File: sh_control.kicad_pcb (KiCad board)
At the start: 2 copper layers, 21 parts, among them J1 USB_PORT_1, J2 USB_Port_2, J3 USB_Port_3, J4 USB_Port_4, U1 FE1.1s, Y1 X322512MSB4SI

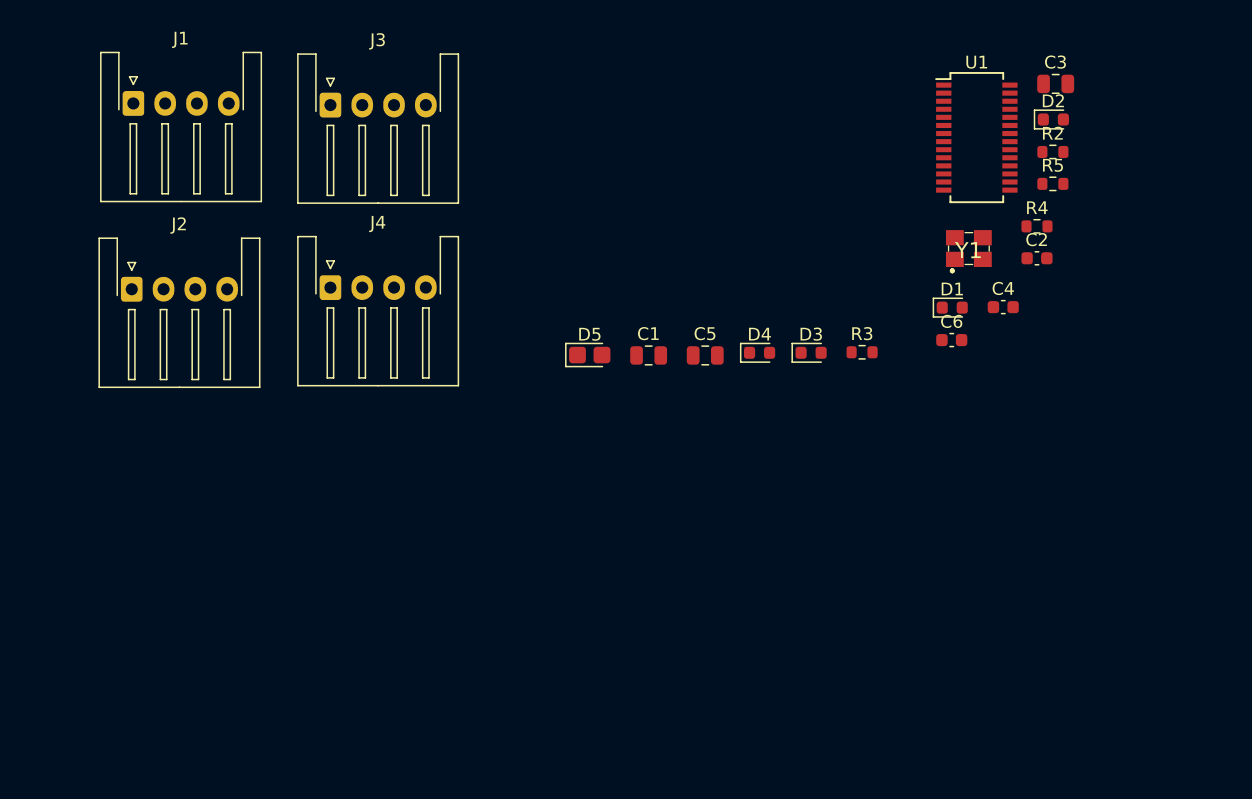
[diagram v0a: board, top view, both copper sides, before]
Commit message: added atmega32 schematic
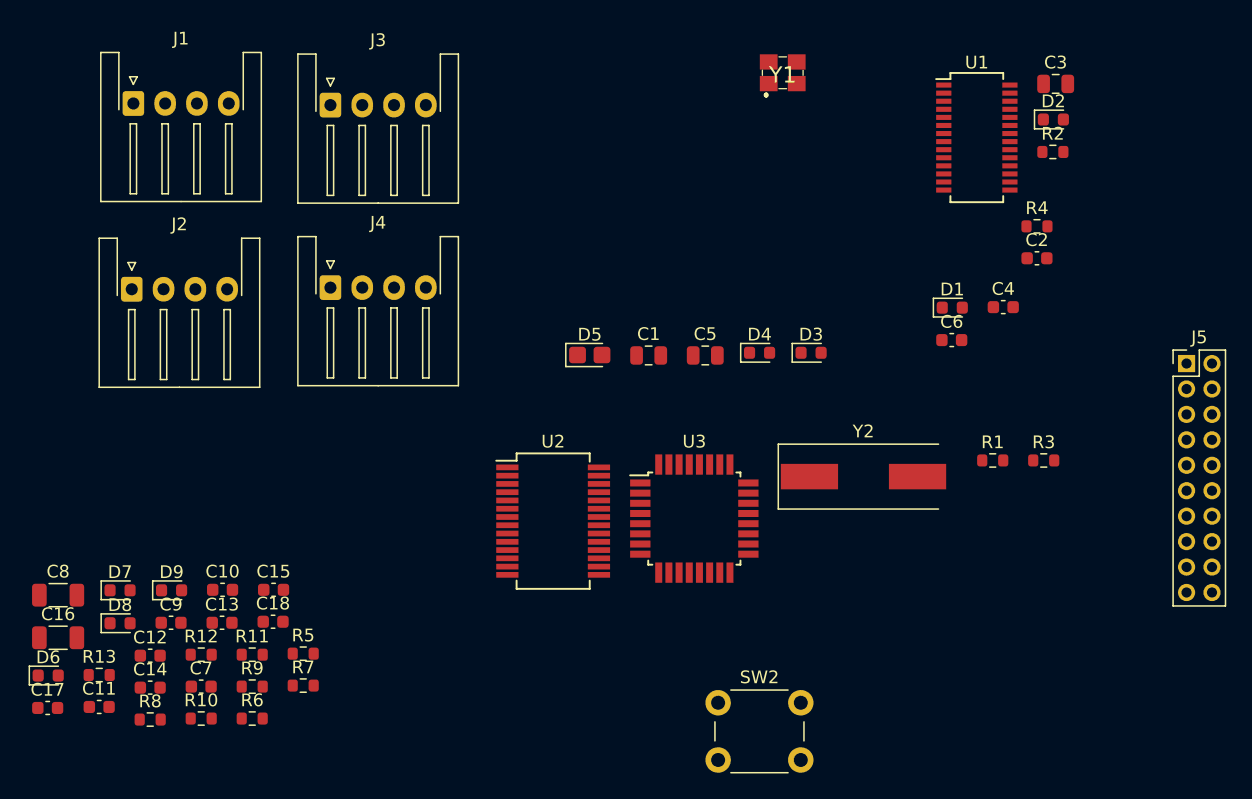
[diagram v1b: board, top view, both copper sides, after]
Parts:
- added C10: 100nF, Capacitor_SMD:C_0603_1608Metric, F.Cu at (113.4, 147.3)
- added C11: 22pF, Capacitor_SMD:C_0603_1608Metric, F.Cu at (103.7, 156.5)
- added C12: 22pF, Capacitor_SMD:C_0603_1608Metric, F.Cu at (107.8, 152.5)
- added C13: 22pF, Capacitor_SMD:C_0603_1608Metric, F.Cu at (113.4, 149.9)
- added C14: 22pF, Capacitor_SMD:C_0603_1608Metric, F.Cu at (107.8, 155.0)
- added C15: 100nF, Capacitor_SMD:C_0603_1608Metric, F.Cu at (117.5, 147.3)
- added C16: 4.7uF, Capacitor_SMD:C_1206_3216Metric, F.Cu at (100.5, 151.1)
- added C17: 100nF, Capacitor_SMD:C_0603_1608Metric, F.Cu at (99.7, 156.6)
- added C18: 100nF, Capacitor_SMD:C_0603_1608Metric, F.Cu at (117.4, 149.8)
- added C7: 100nF, Capacitor_SMD:C_0603_1608Metric, F.Cu at (111.8, 154.9)
- added C8: 4.7uF, Capacitor_SMD:C_1206_3216Metric, F.Cu at (100.5, 147.8)
- added C9: 100nF, Capacitor_SMD:C_0603_1608Metric, F.Cu at (109.4, 149.9)
- added D6: SCK, LED_SMD:LED_0603_1608Metric, F.Cu at (99.7, 154.1)
- added D7: 3V3, LED_SMD:LED_0603_1608Metric, F.Cu at (105.4, 147.4)
- added D8: RX, LED_SMD:LED_0603_1608Metric, F.Cu at (105.4, 150.0)
- added D9: TX, LED_SMD:LED_0603_1608Metric, F.Cu at (109.4, 147.4)
- added J5: Conn_02x10_Odd_Even, Connector_PinHeader_2.00mm:PinHeader_2x10_P2.00mm_Vertical, F.Cu at (189.2, 129.5)
- added R1: 1.5K, Resistor_SMD:R_0603_1608Metric, F.Cu at (174.0, 137.2)
- added R10: 22, Resistor_SMD:R_0603_1608Metric, F.Cu at (111.8, 157.4)
- added R11: 1K, Resistor_SMD:R_0603_1608Metric, F.Cu at (115.8, 152.4)
- added R12: 1K, Resistor_SMD:R_0603_1608Metric, F.Cu at (111.8, 152.4)
- added R13: 1K, Resistor_SMD:R_0603_1608Metric, F.Cu at (103.7, 154.0)
- added R6: 1K, Resistor_SMD:R_0603_1608Metric, F.Cu at (115.8, 157.4)
- added R7: 1K, Resistor_SMD:R_0603_1608Metric, F.Cu at (119.8, 154.9)
- added R8: 1K, Resistor_SMD:R_0603_1608Metric, F.Cu at (107.8, 157.5)
- added R9: 22, Resistor_SMD:R_0603_1608Metric, F.Cu at (115.8, 154.9)
- added SW2: SW_Push_Dual_x2, Button_Switch_THT:SW_PUSH_6mm_H4.3mm, F.Cu at (152.4, 156.2)
- added U2: FT232RL, Package_SO:SSOP-28_5.3x10.2mm_P0.65mm, F.Cu at (139.4, 141.9)
- added U3: ATmega328P-AU, Package_QFP:TQFP-32_7x7mm_P0.8mm, F.Cu at (150.5, 141.7)
- added Y2: Crystal, Crystal:Crystal_SMD_HC49-SD, F.Cu at (163.8, 138.4)
- R3, R4: value 1K -> 1.5K
- Y1: footprint crystal_12MHz:X322512MSB4SI -> max_KiCAD_lib:X322512MSB4SI
- moved R5 69.6 mm to (119.8, 152.3)
- moved Y1 20.1 mm to (157.5, 106.7)
- moved R3 16.6 mm to (178.0, 137.2)
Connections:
- D1 pad 1: Net-(D1-Pad1) -> /USB_HUB/DRV
- D2 pad 2: Net-(D1-Pad1) -> /USB_HUB/DRV
- D3 pad 1: Net-(D1-Pad1) -> /USB_HUB/DRV
- D4 pad 2: Net-(D1-Pad1) -> /USB_HUB/DRV
- D5 pad 1: GND -> Net-(D5-Pad1)
- D5 pad 2: Net-(D5-Pad2) -> /USB_HUB/DRV
- R3 pad 1: Net-(D1-Pad2) -> GND
- R3 pad 2: /USB_HUB/LED1 -> Net-(D5-Pad1)
- R5 pad 1: Net-(D5-Pad2) -> Net-(R5-Pad1)
- R5 pad 2: Net-(D1-Pad1) -> /Atmega32/TXD

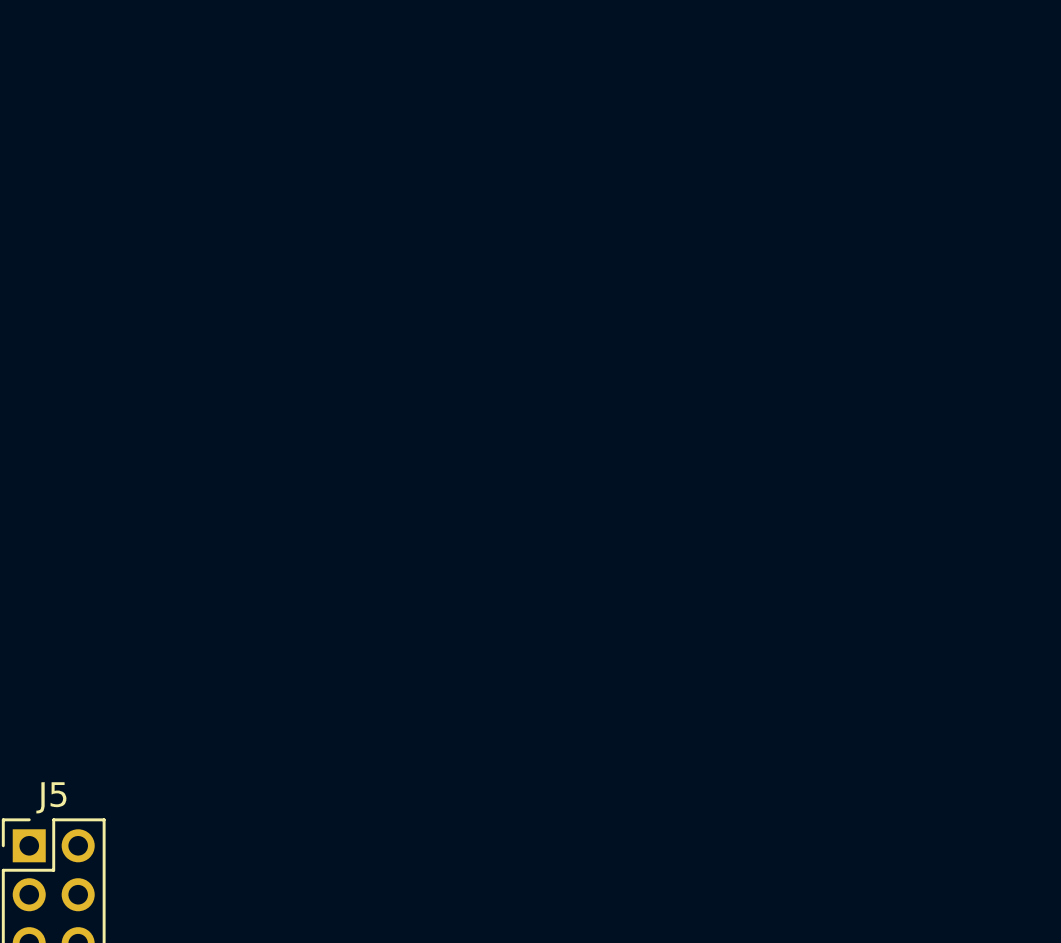
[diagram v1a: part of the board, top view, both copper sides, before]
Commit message: small changes to schematic
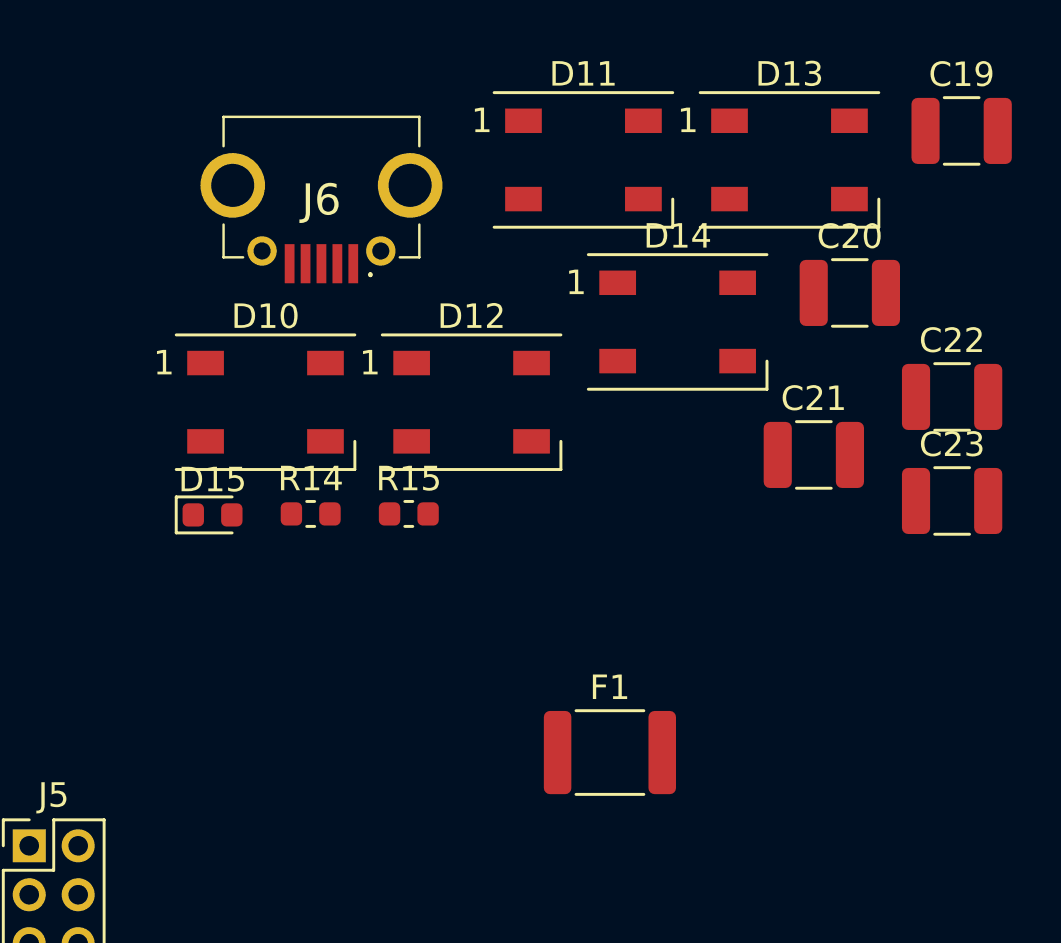
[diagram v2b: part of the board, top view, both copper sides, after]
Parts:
- added C19: 100 uF, Capacitor_SMD:C_1210_3225Metric, F.Cu at (227.3, 100.3)
- added C20: 100 uF, Capacitor_SMD:C_1210_3225Metric, F.Cu at (222.8, 107.0)
- added C21: 100 uF, Capacitor_SMD:C_1210_3225Metric, F.Cu at (221.3, 113.6)
- added C22: 100 uF, Capacitor_SMD:C_1210_3225Metric, F.Cu at (226.9, 111.2)
- added C23: 100 uF, Capacitor_SMD:C_1210_3225Metric, F.Cu at (226.9, 115.5)
- added D10: WS2812B, LED_SMD:LED_WS2812B_PLCC4_5.0x5.0mm_P3.2mm, F.Cu at (198.9, 111.4)
- added D11: WS2812B, LED_SMD:LED_WS2812B_PLCC4_5.0x5.0mm_P3.2mm, F.Cu at (211.9, 101.5)
- added D12: WS2812B, LED_SMD:LED_WS2812B_PLCC4_5.0x5.0mm_P3.2mm, F.Cu at (207.3, 111.4)
- added D13: WS2812B, LED_SMD:LED_WS2812B_PLCC4_5.0x5.0mm_P3.2mm, F.Cu at (220.3, 101.5)
- added D14: WS2812B, LED_SMD:LED_WS2812B_PLCC4_5.0x5.0mm_P3.2mm, F.Cu at (215.7, 108.1)
- added D15: LED_Small, LED_SMD:LED_0603_1608Metric, F.Cu at (196.7, 116.0)
- added F1: 500 mA, Fuse:Fuse_1812_4532Metric, F.Cu at (213.0, 125.7)
- added J6: C10418, max_KiCAD_lib:C10418, F.Cu at (201.2, 102.8)
- added R14: 1.5K, Fuse:Fuse_0603_1608Metric, F.Cu at (200.7, 116.0)
- added R15: 300, Fuse:Fuse_0603_1608Metric, F.Cu at (204.7, 116.0)
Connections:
- C13 pad 1: /Atmega32/D+ -> /Atmega32/D_P
- C14 pad 1: /Atmega32/D- -> /Atmega32/D_N
- J4 pad 3: /USB_HUB/D4_P -> /D4_P
- J4 pad 4: /USB_HUB/D4_N -> /D4_N
- J5 pad 17: Net-(J5-Pad17) -> /D4_P
- J5 pad 18: Net-(J5-Pad18) -> /Atmega32/D_P
- J5 pad 19: Net-(J5-Pad19) -> /D4_N
- J5 pad 20: Net-(J5-Pad20) -> /Atmega32/D_N
- R10 pad 1: /Atmega32/D- -> /Atmega32/D_N
- R9 pad 1: /Atmega32/D+ -> /Atmega32/D_P
- U1 pad 15: /USB_HUB/D_M -> /D_N
- U1 pad 16: /USB_HUB/D_P -> /D_P
- U1 pad 4: /USB_HUB/D4_N -> /D4_N
- U1 pad 5: /USB_HUB/D4_P -> /D4_P
- U3 pad 9: Net-(U3-Pad9) -> /data

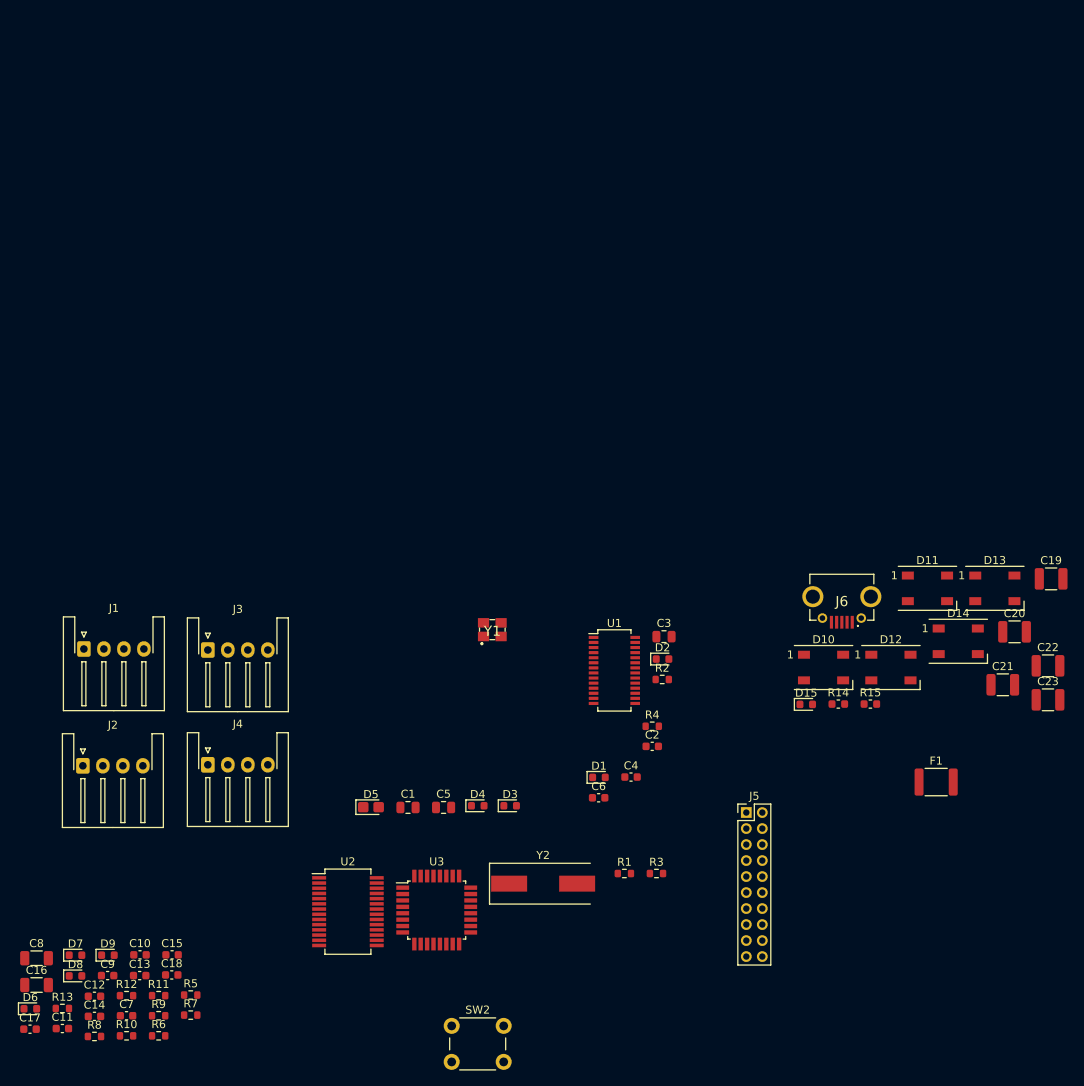
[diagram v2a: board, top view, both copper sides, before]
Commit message: pcb schematic and layout edit i.e. finished -> orderd pcb jlcpcb
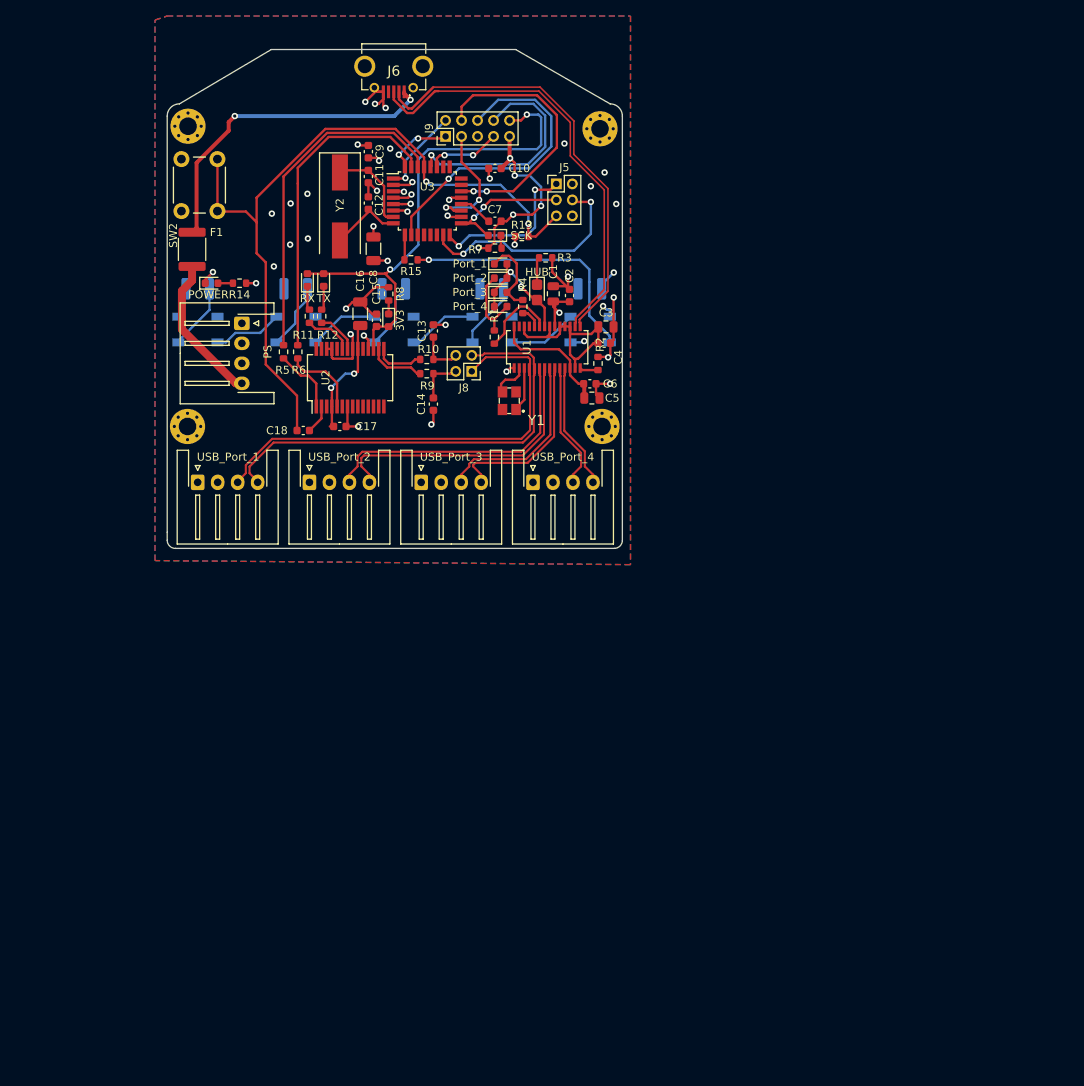
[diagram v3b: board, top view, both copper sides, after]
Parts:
- added J7: PS, Connector_JST:JST_XH_S4B-XH-A-1_1x04_P2.50mm_Horizontal, F.Cu at (126.2, 68.4)
- added J8: Conn_02x02_Odd_Even, Connector_PinHeader_2.00mm:PinHeader_2x02_P2.00mm_Vertical, F.Cu at (154.9, 74.4)
- added J9: Conn_02x05_Odd_Even, Connector_PinHeader_2.00mm:PinHeader_2x05_P2.00mm_Vertical, F.Cu at (151.6, 45.0)
- added TP1: TestPoint, MountingHole:MountingHole_2.2mm_M2_Pad_Via, F.Cu at (171.2, 81.3)
- added TP2: TestPoint, MountingHole:MountingHole_2.2mm_M2_Pad_Via, F.Cu at (170.9, 44.1)
- added TP3: TestPoint, MountingHole:MountingHole_2.2mm_M2_Pad_Via, F.Cu at (119.4, 43.8)
- added TP4: TestPoint, MountingHole:MountingHole_2.2mm_M2_Pad_Via, F.Cu at (119.4, 81.3)
- C19, C20, C21, C22, C23, D10, D11, D12, D13, D14: moved to B.Cu
- D15: value LED_Small -> POWER
- J1: value USB_PORT_1 -> USB_Port_1
- J5: value Conn_02x10_Odd_Even -> Conn_02x03_Odd_Even; footprint Connector_PinHeader_2.00mm:PinHeader_2x10_P2.00mm_Vertical -> Connector_PinHeader_2.00mm:PinHeader_2x03_P2.00mm_Vertical
- R14, R15: footprint Fuse:Fuse_0603_1608Metric -> Resistor_SMD:R_0603_1608Metric
- moved C23 118.1 mm to (120.7, 64.1), turned to 180 degrees
- moved F1 114.4 mm to (120.0, 59.1), turned to 90 degrees
- moved C11 113.2 mm to (142.0, 50.0), turned to 270 degrees
- moved D6 112.8 mm to (157.8, 57.4), turned to 180 degrees
- moved R13 112.3 mm to (161.2, 57.5)
- moved C7 109.5 mm to (157.8, 55.6)
- moved C9 108.0 mm to (142.0, 46.9), turned to 270 degrees
- moved C10 107.9 mm to (157.8, 49.0)
- moved SW2 107.3 mm to (118.6, 54.4), turned to 90 degrees
- moved C22 105.2 mm to (132.9, 64.1), turned to 180 degrees
- moved C12 104.9 mm to (142.0, 53.4), turned to 90 degrees
- moved R7 103.1 mm to (157.8, 59.0), turned to 180 degrees
- moved D14 102.7 mm to (120.7, 69.2)
- moved R8 99.8 mm to (144.5, 64.7), turned to 270 degrees
- moved C8 98.2 mm to (142.6, 59.1), turned to 90 degrees
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- renumbered D7 to 3V3
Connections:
- 3V3 pad 2: +3V3 -> /Atmega32/3V3_ft232rl
- C15 pad 2: +3V3 -> /Atmega32/3V3_ft232rl
- C9 pad 1: GND -> Net-(C9-Pad1)
- C9 pad 2: +5V -> Net-(C9-Pad2)
- D1 pad 1: /USB_HUB/DRV -> Net-(D1-Pad1)
- D1 pad 2: Net-(D1-Pad2) -> /USB_HUB/DRV
- D2 pad 1: Net-(D1-Pad2) -> /USB_HUB/DRV
- D2 pad 2: /USB_HUB/DRV -> Net-(D1-Pad1)
- D3 pad 1: /USB_HUB/DRV -> Net-(D3-Pad1)
- D3 pad 2: Net-(D3-Pad2) -> /USB_HUB/DRV
- D4 pad 1: Net-(D3-Pad2) -> /USB_HUB/DRV
- D4 pad 2: /USB_HUB/DRV -> Net-(D3-Pad1)
- D8 pad 2: +3V3 -> /Atmega32/3V3_ft232rl
- D9 pad 2: +3V3 -> /Atmega32/3V3_ft232rl
- F1 pad 1: +5V -> Net-(F1-Pad1)
- J1 pad 3: /USB_HUB/D1_P -> /D4_N
- J1 pad 4: /USB_HUB/D1_N -> /D4_P
- J2 pad 3: /USB_HUB/D2_P -> /USB_HUB/D3_N
- J2 pad 4: /USB_HUB/D2_N -> /USB_HUB/D3_P
- J3 pad 3: /USB_HUB/D3_P -> /USB_HUB/D2_N
- J3 pad 4: /USB_HUB/D3_N -> /USB_HUB/D2_P
- J4 pad 3: /D4_P -> /USB_HUB/D1_N
- J4 pad 4: /D4_N -> /USB_HUB/D1_P
- R1 pad 1: Net-(D1-Pad2) -> Net-(D3-Pad1)
- R4 pad 1: Net-(D3-Pad2) -> Net-(D1-Pad1)
- U2 pad 17: +3V3 -> /Atmega32/3V3_ft232rl
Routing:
- net GND: track 0.00 -> 95.8 mm, vias 0 -> 37
- net /Atmega32/RESET: track 0.00 -> 94.2 mm, vias 0 -> 2
- net /Atmega32/3V3_ft232rl: track 0.00 -> 62.0 mm, vias 0 -> 2
- net /D4_P: track 0.00 -> 58.1 mm
- net /D4_N: track 0.00 -> 58.0 mm
- net /D_P: track 0.00 -> 55.3 mm
- net /D_N: track 0.00 -> 55.1 mm
- net Net-(R5-Pad1): track 0.00 -> 42.6 mm
- net Net-(F1-Pad2): track 0.00 -> 40.9 mm, vias 0 -> 2
- net Net-(R6-Pad1): track 0.00 -> 40.2 mm
- net /Atmega32/PD6: track 0.00 -> 38.4 mm, vias 0 -> 1
- net +5V: track 0.00 -> 38.2 mm, vias 0 -> 12
- net /USB_HUB/D3_P: track 0.00 -> 36.9 mm
- net /USB_HUB/D3_N: track 0.00 -> 36.9 mm
- net /Atmega32/ADC7: track 0.00 -> 33.5 mm, vias 0 -> 2
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- added copper zone on In1.Cu, net +5V
- added copper zone on B.Cu, net GND
- added copper zone on F.Cu, net GND
- added copper zone on In2.Cu, net GND
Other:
- board outline added: 56.9 x 62.4 mm
- copper layers 2 -> 4
- board text added: "Stiftehalter Max Altrichter V3.5"
